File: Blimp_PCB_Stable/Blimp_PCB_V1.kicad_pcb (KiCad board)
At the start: 2 copper layers, 109.9 x 62 mm, 24 parts, among them J1 S8B-PH-K-S, J2 S4B-XH-A

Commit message: Fixed orientations, added in traces, fixed everything its perfect
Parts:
- added P2: ~, TerminalBlock_Phoenix:TerminalBlock_Phoenix_MKDS-1,5-2_1x02_P5.00mm_Horizontal, B.Cu at (205.4, 83.5)
- B1, J1: moved to B.Cu
- P1: footprint Pins:PWM -> Connector_JST:JST_XH_B2B-XH-A_1x02_P2.50mm_Vertical
- P3: footprint PINS:Shorting Pins -> Connector_JST:JST_XH_B2B-XH-A_1x02_P2.50mm_Vertical
- P9: footprint PINS:Latching Pins -> TerminalBlock_Phoenix:TerminalBlock_Phoenix_MKDS-1,5-2_1x02_P5.00mm_Horizontal; moved to B.Cu
- R1: value 30KΩ -> 30K; moved to B.Cu
- R2: value 7.5KΩ -> 7.5K; moved to B.Cu
- U3: footprint Pins:PWM -> Connector_JST:JST_XH_S2B-XH-A_1x02_P2.50mm_Horizontal
- moved J1 43.8 mm to (144.8, 72.7), turned to 180 degrees
- moved P5 21.3 mm to (197.2, 128.7)
- moved R2 20.2 mm to (193.3, 122.1), turned to -90 degrees
- moved P1 17.2 mm to (190.8, 83.0)
- moved J2 16.5 mm to (178.6, 133.9)
- moved G*** 15.0 mm to (125.6, 123.3)
- moved P9 14.3 mm to (190.3, 99.9)
- moved C3 14.2 mm to (186.7, 83.9), turned to -90 degrees
- moved R1 10.5 mm to (193.3, 115.0), turned to -90 degrees
- moved U2 8.18 mm to (125.0, 99.9)
- moved C2 1.09 mm to (160.2, 123.4)
- moved P8 1.09 mm to (186.2, 72.4)
- moved U3 1.07 mm to (137.4, 127.0)
- moved B1 0.71 mm to (208.2, 99.9), turned to 90 degrees
- moved P3 0.70 mm to (200.7, 112.5)
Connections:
- B1 pad 3: GND -> BV
- B1 pad 4: BV -> GND
- P1 pad 1: (no net) -> +5V
- P1 pad 2: +5V -> GND
- P8 pad 2: unconnected-(P8-5V-Pad2) -> +5V
- P9 pad 1: BV -> GND
- P9 pad 2: GND -> BV
- U3 pad 1: unconnected-(U3-Pad1) -> Net-(P8-SDA.5)
- U3 pad 2: Net-(P8-SDA.5) -> GND
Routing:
- net Net-(P8-SDA.5): track 0.00 -> 101.4 mm
- net Net-(P4-PWM): track 0.00 -> 73.7 mm
- net Net-(P8-TXD.0): track 0.00 -> 70.4 mm
- net Net-(P8-RXD.0): track 0.00 -> 64.1 mm
- net Net-(P8-SPI4_TXD): track 0.00 -> 59.0 mm
- net Net-(P8-SPI4_RXD): track 0.00 -> 59.0 mm
- net BV: track 0.00 -> 47.5 mm
- net +5V: track 0.00 -> 32.9 mm
- net Net-(P5-Pad1): track 0.00 -> 15.1 mm
- net GND: track 0.00 -> 0.64 mm
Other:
- board text added: "${REFERENCE}"
- board text added: "Arik Herzog, Thomas Zachariah"
- board text added: "Arik Herzog, Thomas Zechariah"
- board text removed: "Nate Dickey"

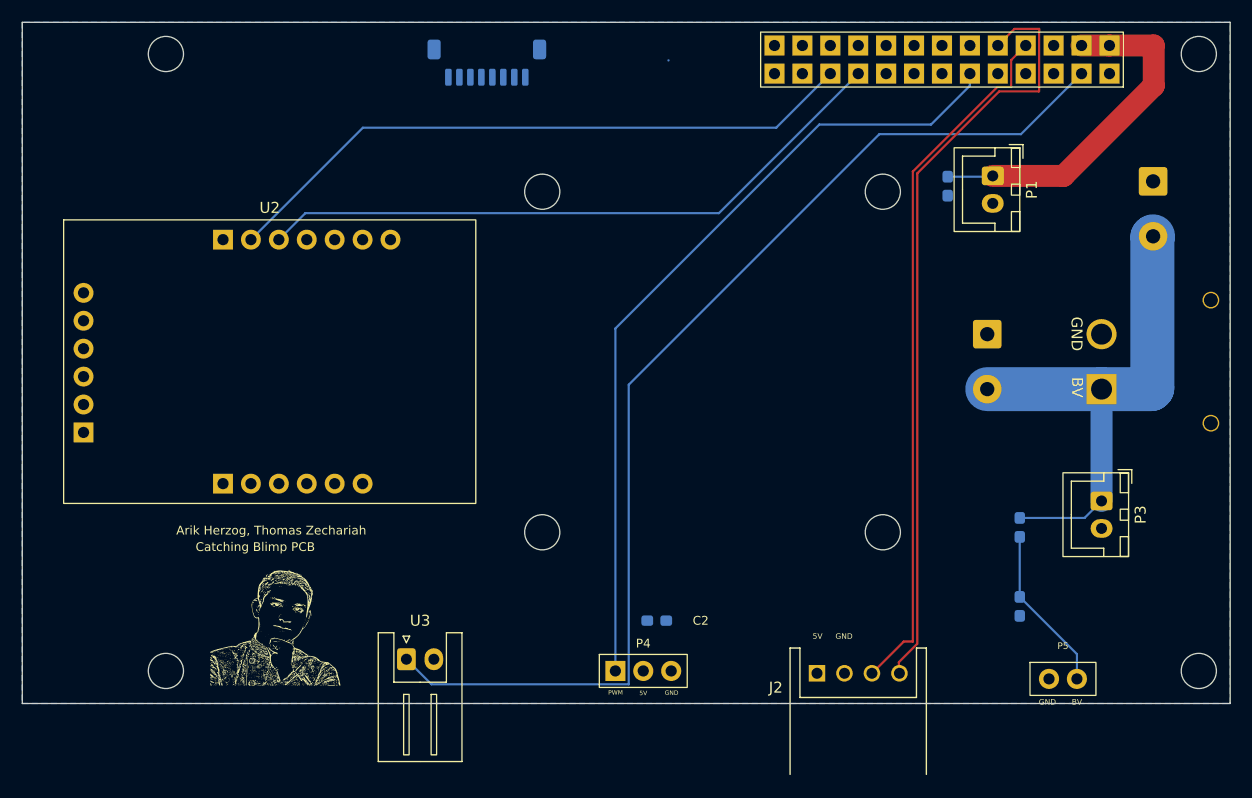
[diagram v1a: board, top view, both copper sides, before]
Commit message: Added ground plane and connected everything up to it, might need to review trace sizes, connected JST 8pin to ESC signals, connected 3.3V from orangepi to IMU
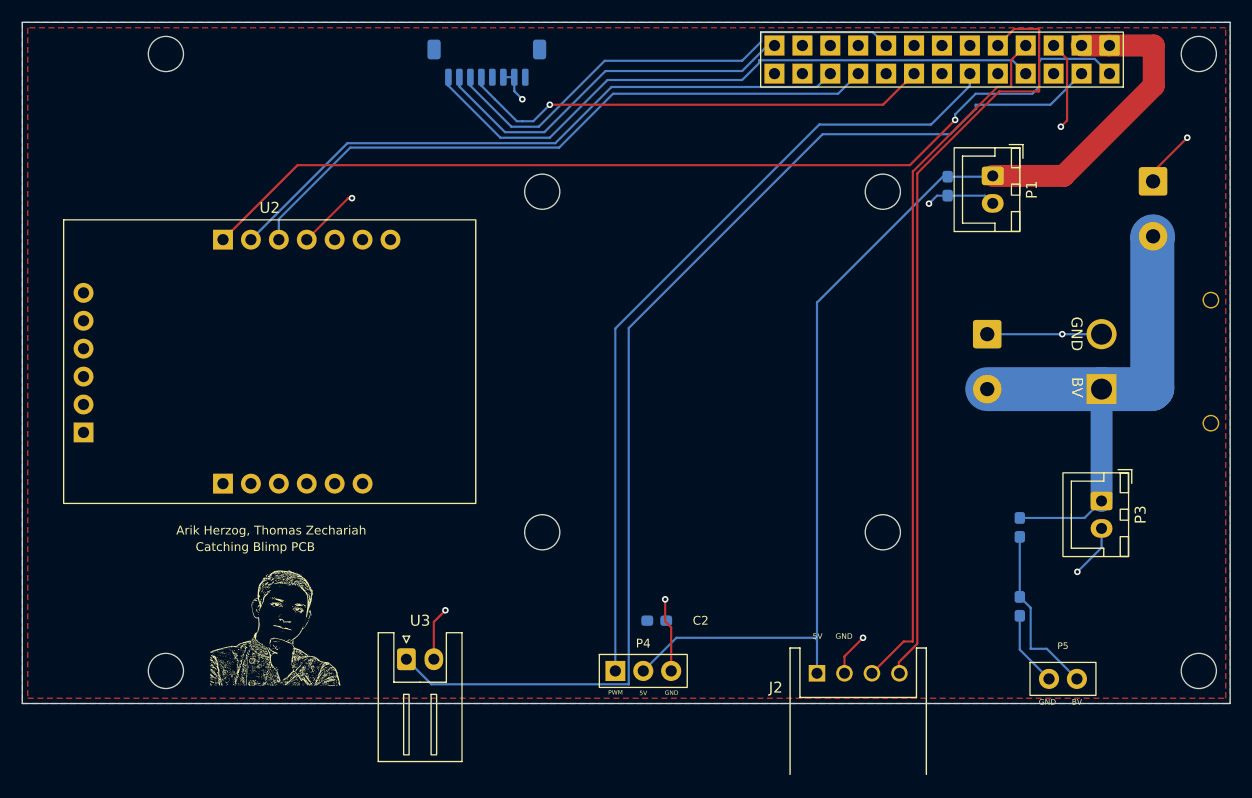
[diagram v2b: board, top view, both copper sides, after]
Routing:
- net +3.3V: track 0.02 -> 89.7 mm, vias 0 -> 1
- net +5V: track 32.9 -> 99.9 mm
- net GND: track 0.64 -> 67.1 mm, vias 0 -> 10
- net Net-(P8-PWM15): track 0.00 -> 58.8 mm
- net Net-(P8-SCL.1): track 0.00 -> 45.2 mm
- net Net-(P8-CAN2_RX): track 0.00 -> 43.3 mm, vias 0 -> 1
- net Net-(P8-PWM1): track 0.00 -> 34.5 mm
- net Net-(P8-SDA.5): track 101.4 -> 105.1 mm
- net Net-(P8-SPI4_TXD): track 59.0 -> 60.1 mm
- net Net-(P5-Pad1): track 15.1 -> 15.9 mm
- added copper zone on F.Cu, net GND

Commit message: fixed unnecessary vias, streamlined traces
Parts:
- moved C2 0.36 mm to (159.9, 123.4)
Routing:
- net GND: track 67.1 -> 26.3 mm, vias 10 -> 4
- net Net-(P8-SDA.5): track 105.1 -> 89.8 mm, vias 0 -> 1
- net +5V: track 99.9 -> 103.4 mm
- net BV: track 47.5 -> 50.4 mm

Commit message: quick fix
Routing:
- net Net-(P8-TXD.0): track 70.4 -> 63.1 mm
- net Net-(P8-RXD.0): track 64.1 -> 66.8 mm
- net +3.3V: track 89.7 -> 87.0 mm
- net Net-(P4-PWM): track 73.9 -> 74.9 mm
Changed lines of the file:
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@@
+	)
+	(segment
+		(start 197.558 72.326)
+		(end 197.558 76.067)
+		(width 0.2)
+		(layer "F.Cu")
+		(net 1)
 	)
 	(segment
@@
 	)
 	(segment
+		(start 197.558 76.067)
+		(end 197.075 76.55)
+		(width 0.2)
+		(layer "F.Cu")
+		(net 1)
+	)
+	(segment
 		(start 139.95 126.95)
 		(end 139.95 123.55)
@@
 		(start 205.39 83.47)
 		(end 205.39 82.61)
-		(width 0.2)
-		(layer "F.Cu")
-		(net 1)
-	)
-	(segment
-		(start 197.558 72.326)
-		(end 197.558 76.442)
 		(width 0.2)
 		(layer "F.Cu")
@@
 	)
 	(segment
-		(start 185.51147 79.75)
+		(start 178.526 79.75)
 		(end 129.7909 79.75)
 		(width 0.2)
@@
 		(net 11)
 	)
-	(segment
-		(start 186.75 78.51147)
-		(end 185.51147 79.75)
-		(width 0.2)
-		(layer "F.Cu")
-		(net 11)
-	)
-	(segment
-		(start 186.75 78)
-		(end 186.75 78.51147)
-		(width 0.2)
-		(layer "F.Cu")
-		(net 11)
-	)
 	(via
-		(at 186.75 78)
+		(at 178.526 79.75)
 		(size 0.6)
 		(drill 0.3)
@@
 	)
 	(segment
-		(start 200.078 72.326)
+		(start 178.526 79.75)
+		(end 179.224 79.052)
+		(width 0.2)
+		(layer "B.Cu")
+		(net 11)
+	)
+	(segment
+		(start 198.2191 74.9)
+		(end 200.192 74.9)
+		(width 0.2)
+		(layer "B.Cu")
+		(net 11)
+	)
+	(segment
+		(start 201.422 73.778)
 		(end 201.422 73.67)
 		(width 0.2)
@@
 	)
 	(segment
-		(start 195.018 72.562)
-		(end 195.254 72.326)
-		(width 0.2)
-		(layer "B.Cu")
-		(net 11)
-	)
-	(segment
-		(start 186.75 78)
-		(end 189.5 75.25)
-		(width 0.2)
-		(layer "B.Cu")
-		(net 11)
-	)
-	(segment
-		(start 189.5 75.25)
-		(end 194.654 75.25)
-		(width 0.2)
-		(layer "B.Cu")
-		(net 11)
-	)
-	(segment
-		(start 194.654 75.25)
-		(end 195.018 74.886)
-		(width 0.2)
-		(layer "B.Cu")
-		(net 11)
-	)
-	(segment
-		(start 195.018 74.886)
-		(end 195.018 72.562)
-		(width 0.2)
-		(layer "B.Cu")
-		(net 11)
-	)
-	(segment
-		(start 195.254 72.326)
-		(end 200.078 72.326)
-		(width 0.2)
-		(layer "B.Cu")
-		(net 11)
+		(start 196.9681 76.151)
+		(end 198.2191 74.9)
+		(width 0.2)
+		(layer "B.Cu")
+		(net 11)
+	)
+	(segment
+		(start 200.192 74.9)
+		(end 201.422 73.67)
+		(width 0.2)
+		(layer "B.Cu")
+		(net 11)
+	)
+	(segment
+		(start 179.224 79.052)
+		(end 187.626513 79.052)
+		(width 0.2)
+		(layer "B.Cu")
+		(net 11)
+	)
+	(segment
+		(start 187.626513 79.052)
+		(end 190.527513 76.151)
+		(width 0.2)
+		(layer "B.Cu")
+		(net 11)
+	)
+	(segment
+		(start 190.527513 76.151)
+		(end 196.9681 76.151)
+		(width 0.2)
+		(layer "B.Cu")
+		(net 11)
+	)
+	(segment
+		(start 188.722 76.822313)
+		(end 188.722 73.67)
+		(width 0.2)
+		(layer "B.Cu")
+		(net 22)
+	)
+	(segment
+		(start 187.294313 78.25)
+		(end 188.722 76.822313)
+		(width 0.2)
+		(layer "B.Cu")
+		(net 22)
+	)
+	(segment
+		(start 175.072 78.25)
+		(end 187.294313 78.25)
+		(width 0.2)
+		(layer "B.Cu")
+		(net 22)
+	)
+	(segment
+		(start 156.464 128.016)
+		(end 156.464 96.858)
+		(width 0.2)
+		(layer "B.Cu")
+		(net 22)
 	)
 	(segment
 		(start 156.464 96.858)
 		(end 175.072 78.25)
-		(width 0.2)
-		(layer "B.Cu")
-		(net 22)
-	)
-	(segment
-		(start 185.650057 78.25)
-		(end 188.722 75.178057)
-		(width 0.2)
-		(layer "B.Cu")
-		(net 22)
-	)
-	(segment
-		(start 175.072 78.25)
-		(end 185.650057 78.25)
-		(width 0.2)
-		(layer "B.Cu")
-		(net 22)
-	)
-	(segment
-		(start 156.464 128.016)
-		(end 156.464 96.858)
-		(width 0.2)
-		(layer "B.Cu")
-		(net 22)
-	)
-	(segment
-		(start 188.722 75.178057)
-		(end 188.722 73.67)
 		(width 0.2)
 		(layer "B.Cu")
@@
 	)
 	(segment
+		(start 196.802 75.75)
+		(end 198.882 73.67)
+		(width 0.2)
+		(layer "B.Cu")
+		(net 34)
+	)
+	(segment
+		(start 159 97.25)
+		(end 159 95.5)
+		(width 0.2)
+		(layer "B.Cu")
+		(net 34)
+	)
+	(segment
+		(start 175.849 78.651)
+		(end 187.460413 78.651)
+		(width 0.2)
+		(layer "B.Cu")
+		(net 34)
+	)
+	(segment
+		(start 159 95.5)
+		(end 175.849 78.651)
+		(width 0.2)
+		(layer "B.Cu")
+		(net 34)
+	)
+	(segment
 		(start 190.361413 75.75)
 		(end 196.802 75.75)
@@
 	)
 	(segment
-		(start 159 95.5)
-		(end 175.32 79.18)
-		(width 0.2)
-		(layer "B.Cu")
-		(net 34)
-	)
-	(segment
-		(start 159 97.25)
-		(end 159 95.5)
-		(width 0.2)
-		(layer "B.Cu")
-		(net 34)
-	)
-	(segment
-		(start 175.32 79.18)
-		(end 186.931413 79.18)
+		(start 187.460413 78.651)
+		(end 190.361413 75.75)
 		(width 0.2)
 		(layer "B.Cu")
@@
 	)
 	(segment
-		(start 196.802 75.75)
-		(end 198.882 73.67)
-		(width 0.2)
-		(layer "B.Cu")
-		(net 34)
-	)
-	(segment
-		(start 186.931413 79.18)
-		(end 190.361413 75.75)
-		(width 0.2)
-		(layer "B.Cu")
-		(net 34)
-	)
-	(segment
 		(start 176.022 73.67)
 		(end 174.593 75.099)
@@
 	)
 	(segment
-		(start 182.26145 127.21855)
-		(end 182.26 127.2171)
+		(start 190.426 76.2511)
+		(end 183.931 82.7461)
 		(width 0.2)
 		(layer "F.Cu")
@@
 	(segment
 		(start 183.931 82.7461)
-		(end 183.931 125.549)
+		(end 183.931 125.5111)
 		(width 0.2)
 		(layer "F.Cu")
@@
 	)
 	(segment
-		(start 195.03 69.882)
-		(end 195.018 69.894)
+		(start 192.478 75.375)
+		(end 190.426 75.375)
 		(width 0.2)
 		(layer "F.Cu")
@@
 	)
 	(segment
-		(start 195.03 69.601)
-		(end 195.03 69.882)
-		(width 0.2)
-		(layer "F.Cu")
-		(net 44)
-	)
-	(segment
-		(start 182.26145 127.21855)
-		(end 182.26145 128.18145)
-		(width 0.2)
-		(layer "F.Cu")
-		(net 44)
-	)
-	(segment
-		(start 195.018 69.894)
-		(end 195.018 75.26)
+		(start 183.931 125.5111)
+		(end 182.31 127.1321)
 		(width 0.2)
 		(layer "F.Cu")
@@
 	)
 	(segment
-		(start 192.771 69.601)
-		(end 195.03 69.601)
+		(start 190.426 75.375)
+		(end 190.426 76.2511)
 		(width 0.2)
 		(layer "F.Cu")
@@
 	)
 	(segment
-		(start 183.931 125.549)
-		(end 182.26145 127.21855)
+		(start 182.31 127.1321)
+		(end 182.31 128.23)
 		(width 0.2)
 		(layer "F.Cu")
@@
 	)
 	(segment
-		(start 191.3901 75.287)
-		(end 183.931 82.7461)
+		(start 191.262 71.11)
+		(end 192.478 72.326)
 		(width 0.2)
 		(layer "F.Cu")
@@
 	)
 	(segment
-		(start 195.018 75.26)
-		(end 194.991 75.287)
+		(start 192.478 72.326)
+		(end 192.478 75.375)
 		(width 0.2)
 		(layer "F.Cu")
@@
 	)
 	(segment
-		(start 191.262 71.11)
-		(end 192.771 69.601)
-		(width 0.2)
-		(layer "F.Cu")
-		(net 44)
-	)
-	(segment
-		(start 194.991 75.287)
-		(end 191.3901 75.287)
-		(width 0.2)
-		(layer "F.Cu")
-		(net 44)
-	)
-	(segment
-		(start 183.53 125.34)
+		(start 190.046 69.894)
+		(end 192.586 69.894)
+		(width 0.2)
+		(layer "F.Cu")
+		(net 45)
+	)
+	(segment
+		(start 183.53 82.58)
+		(end 190.025 76.085)
+		(width 0.2)
+		(layer "F.Cu")
+		(net 45)
+	)
+	(segment
+		(start 192.586 69.894)
+		(end 193.802 71.11)
+		(width 0.2)
+		(layer "F.Cu")
+		(net 45)
+	)
+	(segment
+		(start 183.53 123.745)
 		(end 183.53 82.58)
 		(width 0.2)
@@
 	)
 	(segment
-		(start 192.478 74.886)
-		(end 192.478 72.434)
+		(start 190.025 76.085)
+		(end 190.025 69.915)
 		(width 0.2)
 		(layer "F.Cu")
@@
 	)
 	(segment
-		(start 191.224 74.886)
-		(end 192.478 74.886)
+		(start 179.81 128.23)
+		(end 179.81 127.465)
 		(width 0.2)
 		(layer "F.Cu")
@@
 	)
 	(segment
-		(start 183.53 125.34)
-		(end 182.7 125.34)
+		(start 179.81 127.465)
+		(end 183.53 123.745)
 		(width 0.2)
 		(layer "F.Cu")
@@
 	)
 	(segment
-		(start 192.478 72.434)
-		(end 193.802 71.11)
-		(width 0.2)
-		(layer "F.Cu")
-		(net 45)
-	)
-	(segment
-		(start 182.7 125.34)
-		(end 179.81 128.23)
-		(width 0.2)
-		(layer "F.Cu")
-		(net 45)
-	)
-	(segment
-		(start 183.53 82.58)
-		(end 191.224 74.886)
-		(width 0.2)
-		(layer "F.Cu")
+		(start 190.025 69.915)
+		(end 190.046 69.894)
+		(width 0.2)
+		(layer "F.Cu")

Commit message: Merged Arik stable update into main
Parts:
- removed J2: S4B-XH-A, S4B_XH_A:JST_S4B-XH-A
- removed R1: 30K, Capacitor_SMD:C_0603_1608Metric_Pad1.08x0.95mm_HandSolder
- removed R2: 7.5K, Capacitor_SMD:C_0603_1608Metric_Pad1.08x0.95mm_HandSolder
- added ?: , , F.Cu at (141.7, 91.2)
- added ?: , , F.Cu at (165.9, 89.9)
- added ?: , , F.Cu at (141.2, 108.5)
- added ?: , , F.Cu at (165.9, 109.0)
- B1: moved to F.Cu
- J1: footprint Connector_JST:JST_SH_BM08B-SRSS-TB_1x08-1MP_P1.00mm_Vertical -> JST Connector:S8B-PH-K-S
- P1: footprint Connector_JST:JST_XH_B2B-XH-A_1x02_P2.50mm_Vertical -> PINS:PWM
- P2: footprint TerminalBlock_Phoenix:TerminalBlock_Phoenix_MKDS-1,5-2_1x02_P5.00mm_Horizontal -> PINS:PWM; moved to F.Cu
- P3: footprint Connector_JST:JST_XH_B2B-XH-A_1x02_P2.50mm_Vertical -> PINS:Shorting Pins
- P9: footprint TerminalBlock_Phoenix:TerminalBlock_Phoenix_MKDS-1,5-2_1x02_P5.00mm_Horizontal -> PINS:Latching Pins; moved to F.Cu
- U3: footprint Connector_JST:JST_XH_S2B-XH-A_1x02_P2.50mm_Horizontal -> Pins:PWM
- moved B1 101.6 mm to (106.6, 100.5)
- moved P3 92.1 mm to (114.3, 80.8)
- moved P5 86.2 mm to (122.8, 85.2)
- moved P9 69.7 mm to (120.7, 100.3)
- moved U2 62.3 mm to (187.3, 98.8)
- moved P1 60.0 mm to (131.1, 77.0)
- moved J1 47.1 mm to (124.7, 115.3), turned to -90 degrees
- moved P2 45.6 mm to (195.8, 128.0), turned to 0 degrees
- moved C3 42.0 mm to (197.5, 124.5), turned to 0 degrees
- moved G*** 15.0 mm to (111.6, 117.9)
- moved ? 15.0 mm to (134.9, 114.6)
- moved ? 15.0 mm to (165.9, 114.6)
- moved ? 15.0 mm to (134.9, 83.6)
- moved ? 15.0 mm to (165.9, 83.6)
- moved C2 1.23 mm to (160.5, 124.5)
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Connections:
- B1 pad 3: BV -> GND
- B1 pad 4: GND -> BV
- P1 pad 1: +5V -> unconnected-(P1-X-Pad1)
- P1 pad 2: GND -> +5V
- P2 pad 1: GND -> unconnected-(P2-PWM-Pad1)
- P2 pad 2: BV -> +5V
- P5 pad 1: Net-(P5-Pad1) -> BV
- P8 pad 10: Net-(P8-TXD.0) -> unconnected-(P8-TXD.0-Pad10)
- P8 pad 2: +5V -> unconnected-(P8-5V-Pad2)
- P8 pad 8: Net-(P8-RXD.0) -> unconnected-(P8-RXD.0-Pad8)
- P9 pad 1: GND -> BV
- P9 pad 2: BV -> GND
- U3 pad 1: Net-(P8-SDA.5) -> unconnected-(U3-Pad1)
- U3 pad 2: GND -> Net-(P8-SDA.5)
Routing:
- net +5V: track 103.4 -> 17.4 mm, vias 0 -> 2
- net Net-(P8-RXD.0): track 66.8 -> 0.00 mm
- net Net-(P8-TXD.0): track 63.1 -> 0.00 mm
- net +3.3V: track 87.0 -> 26.7 mm, vias 1 -> 0
- net Net-(P8-PWM1): track 34.5 -> 85.2 mm, vias 0 -> 2
- net Net-(P8-SDA.5): track 89.8 -> 138.3 mm, vias 1 -> 0
- net Net-(P8-PWM15): track 58.7 -> 104.6 mm, vias 0 -> 1
- net GND: track 26.7 -> 69.8 mm, vias 4 -> 11
- net Net-(P8-SPI4_TXD): track 60.1 -> 17.9 mm
- net Net-(P8-SPI4_RXD): track 59.3 -> 17.9 mm
- net Net-(P8-CAN2_RX): track 43.3 -> 76.6 mm
- net Net-(P8-SCL.1): track 45.2 -> 77.4 mm
- net BV: track 50.4 -> 33.2 mm
- net Net-(P5-Pad1): track 16.4 -> 0.00 mm
- net Net-(P4-PWM): track 74.9 -> 81.7 mm, vias 0 -> 1
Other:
- board text added: "3-Pin ESC"
- board text added: "5V"
- board text added: "GND"
- board text added: "Gnd"
- board text added: "IMU"
- board text added: "Input Pins for BEC"
- board text added: "JST-8"
- board text added: "Latch Pins"
- board text added: "Nate Dickey"
- board text added: "OPI"
- board text added: "Output Pins for BEC"
- board text added: "PINS"
- board text added: "PWM"
- board text removed: "${REFERENCE}"
- board text removed: "Arik Herzog, Thomas Zachariah"
- board text removed: "Arik Herzog, Thomas Zechariah"

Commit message: Arik stable update
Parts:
- removed the ? at (141.7, 91.2)
- removed the ? at (165.9, 89.9)
- removed the ? at (141.2, 108.5)
- removed the ? at (165.9, 109.0)
- added J2: S4B-XH-A, S4B_XH_A:JST_S4B-XH-A, F.Cu at (178.6, 133.9)
- added R1: 30K, Capacitor_SMD:C_0603_1608Metric_Pad1.08x0.95mm_HandSolder, B.Cu at (193.3, 115.0)
- added R2: 7.5K, Capacitor_SMD:C_0603_1608Metric_Pad1.08x0.95mm_HandSolder, B.Cu at (193.3, 122.1)
- B1: moved to B.Cu
- J1: footprint JST Connector:S8B-PH-K-S -> Connector_JST:JST_SH_BM08B-SRSS-TB_1x08-1MP_P1.00mm_Vertical
- P1: footprint PINS:PWM -> Connector_JST:JST_XH_B2B-XH-A_1x02_P2.50mm_Vertical
- P2: footprint PINS:PWM -> TerminalBlock_Phoenix:TerminalBlock_Phoenix_MKDS-1,5-2_1x02_P5.00mm_Horizontal; moved to B.Cu
- P3: footprint PINS:Shorting Pins -> Connector_JST:JST_XH_B2B-XH-A_1x02_P2.50mm_Vertical
- P9: footprint PINS:Latching Pins -> TerminalBlock_Phoenix:TerminalBlock_Phoenix_MKDS-1,5-2_1x02_P5.00mm_Horizontal; moved to B.Cu
- U3: footprint Pins:PWM -> Connector_JST:JST_XH_S2B-XH-A_1x02_P2.50mm_Horizontal
- moved B1 101.6 mm to (208.2, 99.9)
- moved P3 92.1 mm to (200.7, 112.5)
- moved P5 86.0 mm to (197.2, 128.2)
- moved P9 69.7 mm to (190.3, 99.9)
- moved U2 62.3 mm to (125.0, 99.9)
- moved P1 60.0 mm to (190.8, 83.0)
- moved J1 47.1 mm to (144.8, 72.7), turned to 180 degrees
- moved P2 45.6 mm to (205.4, 83.5), turned to -90 degrees
- moved C3 42.0 mm to (186.7, 83.9), turned to -90 degrees
- moved G*** 15.0 mm to (125.6, 123.3)
- moved ? 15.0 mm to (149.8, 115.4)
- moved ? 15.0 mm to (180.8, 115.4)
- moved ? 15.0 mm to (149.8, 84.4)
- moved ? 15.0 mm to (180.8, 84.4)
- moved C2 1.23 mm to (159.9, 123.4)
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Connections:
- B1 pad 3: GND -> BV
- B1 pad 4: BV -> GND
- P1 pad 1: unconnected-(P1-X-Pad1) -> +5V
- P1 pad 2: +5V -> GND
- P2 pad 1: unconnected-(P2-PWM-Pad1) -> GND
- P2 pad 2: +5V -> BV
- P5 pad 1: BV -> Net-(P5-Pad1)
- P8 pad 10: unconnected-(P8-TXD.0-Pad10) -> Net-(P8-TXD.0)
- P8 pad 2: unconnected-(P8-5V-Pad2) -> +5V
- P8 pad 25: unconnected-(P8-GND-Pad25) -> GND
- P8 pad 6: GND -> unconnected-(P8-GND-Pad6)
- P8 pad 8: unconnected-(P8-RXD.0-Pad8) -> Net-(P8-RXD.0)
- P8 pad 9: unconnected-(P8-GND-Pad9) -> GND
- P9 pad 1: BV -> GND
- P9 pad 2: GND -> BV
- U3 pad 1: unconnected-(U3-Pad1) -> Net-(P8-SDA.5)
- U3 pad 2: Net-(P8-SDA.5) -> GND
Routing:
- net +5V: track 17.4 -> 103.4 mm, vias 2 -> 0
- net Net-(P8-RXD.0): track 0.00 -> 69.8 mm
- net Net-(P8-TXD.0): track 0.00 -> 62.3 mm
- net +3.3V: track 26.7 -> 87.0 mm, vias 0 -> 1
- net Net-(P8-PWM1): track 85.2 -> 34.5 mm, vias 2 -> 0
- net GND: track 69.8 -> 22.0 mm, vias 11 -> 4
- net Net-(P8-SDA.5): track 138.3 -> 91.1 mm, vias 0 -> 1
- net Net-(P8-PWM15): track 104.6 -> 58.7 mm, vias 1 -> 0
- net Net-(P8-SPI4_TXD): track 17.9 -> 60.1 mm
- net Net-(P8-SPI4_RXD): track 17.9 -> 59.3 mm
- net Net-(P8-CAN2_RX): track 76.6 -> 43.3 mm
- net Net-(P8-SCL.1): track 77.4 -> 45.2 mm
- net Net-(P5-Pad1): track 0.00 -> 15.8 mm
- net BV: track 33.2 -> 47.2 mm
- net Net-(P4-PWM): track 81.7 -> 74.9 mm, vias 1 -> 0
- removed copper zone on B.Cu, net +5V
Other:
- board text added: "${REFERENCE}"
- board text added: "Arik Herzog, Thomas Zachariah"
- board text added: "Arik Herzog, Thomas Zechariah"
- board text removed: "3-Pin ESC"
- board text removed: "5V"
- board text removed: "GND"
- board text removed: "Gnd"
- board text removed: "IMU"
- board text removed: "Input Pins for BEC"
- board text removed: "JST-8"
- board text removed: "Latch Pins"
- board text removed: "Nate Dickey"
- board text removed: "OPI"
- board text removed: "Output Pins for BEC"
- board text removed: "PINS"
- board text removed: "PWM"
